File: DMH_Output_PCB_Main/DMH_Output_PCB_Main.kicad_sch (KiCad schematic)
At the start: 14 parts, among them J1 TS_Jack_6.35mm_Sw, J2 TS_Jack_6.35mm_Sw, J200 IDC_02x05, J21 Conn_01x02, J22 Conn_01x02, J24 Conn_01x02, J25 Conn_01x02, J3 TRS Jack 6.35mm, J4 TRS Jack 6.35mm, J5 TRS Jack 6.35mm, J6 TS_Jack_6.35mm_Sw, J7 TS_Jack_6.35mm_Sw, J8 TS_Jack_6.35mm_Sw, J9 TS_Jack_6.35mm_Sw

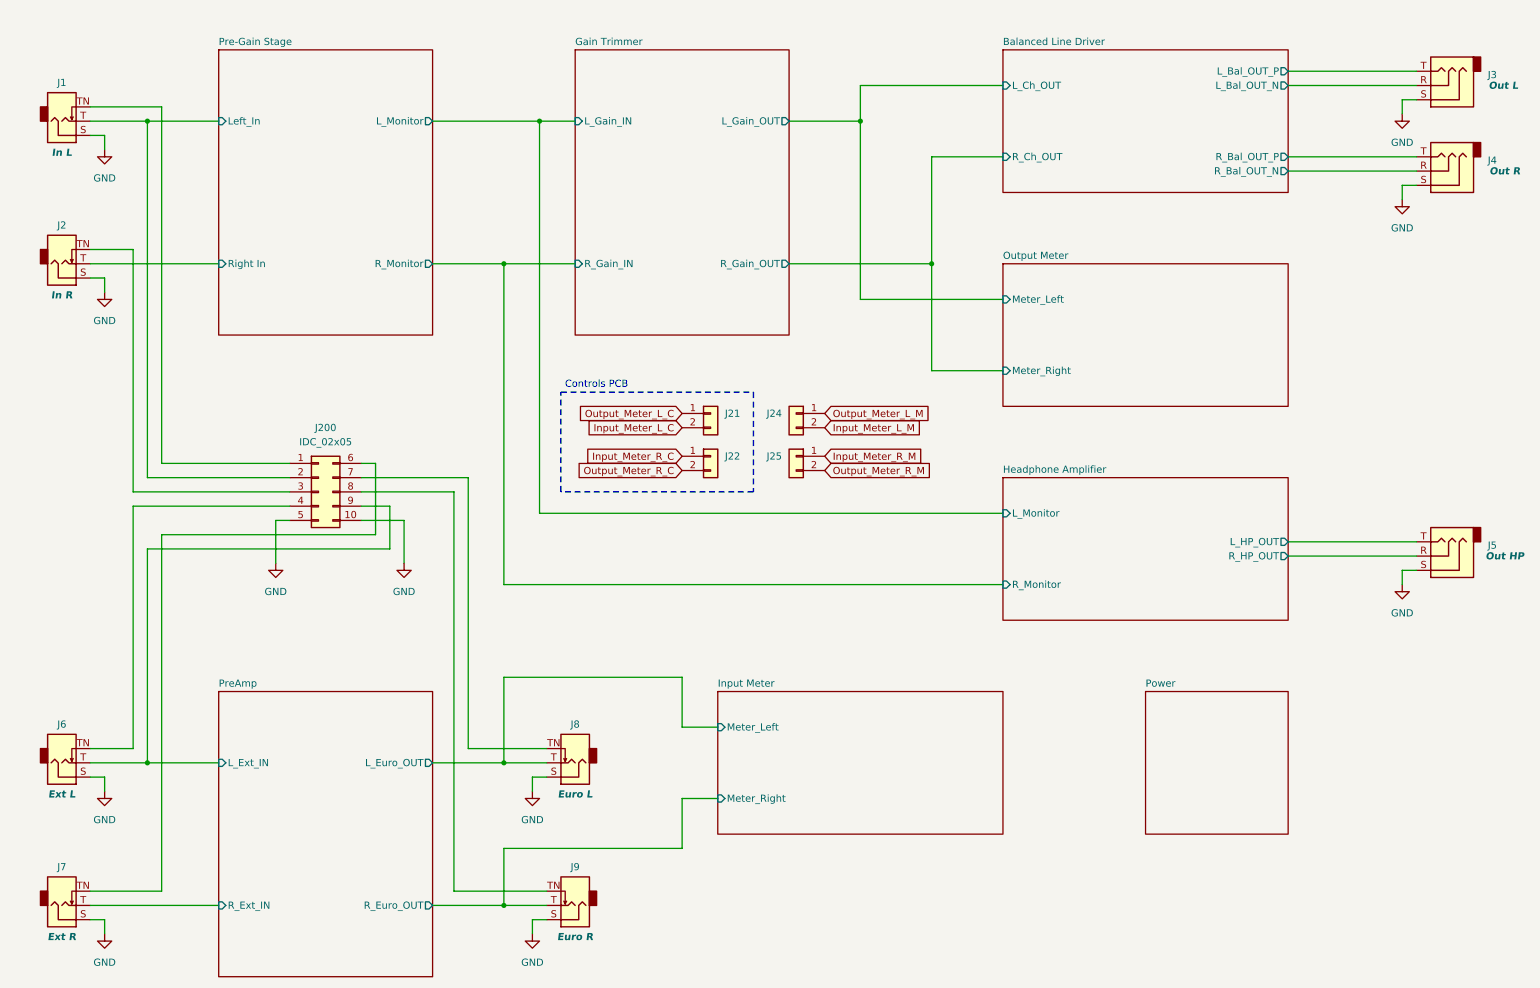
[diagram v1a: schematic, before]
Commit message: Replaced jack symbols with 5pin ones
Also updated Meter LED current source resistor to 75R
Also increased LED guiding PCB mounting holes to M2.5
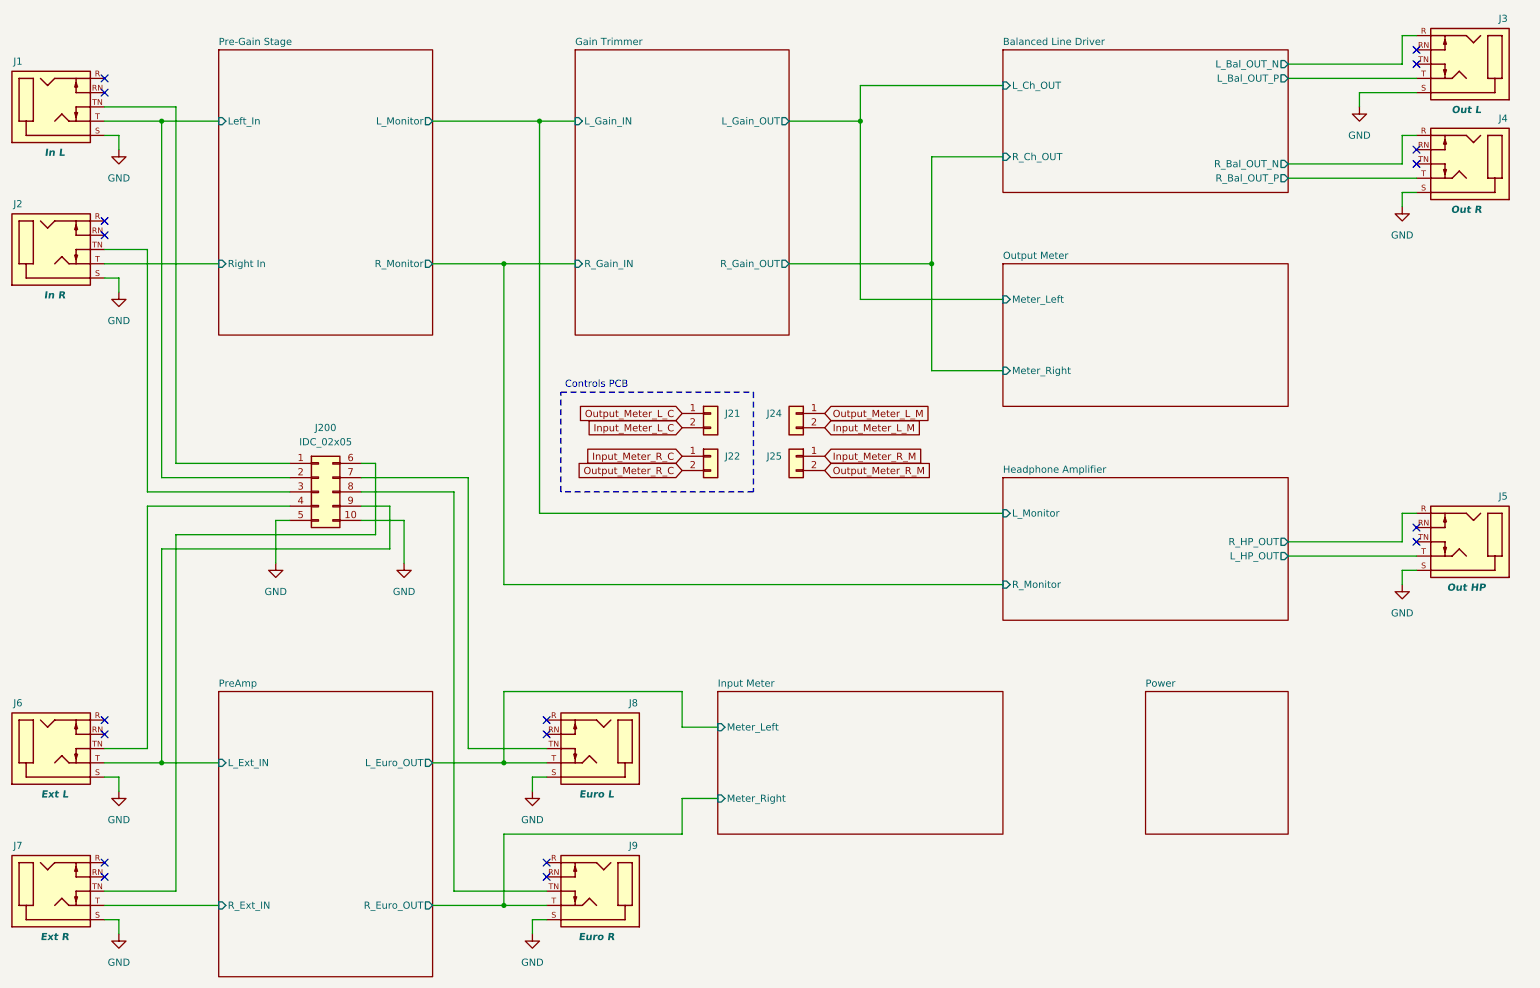
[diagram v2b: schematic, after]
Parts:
- J1, J2, J6, J7, J8, J9: value TS_Jack_6.35mm_Sw -> TRS_Jack_6.35mm_Sw; footprint SynthStuff:CUI_MJ-63052A -> SynthStuff:CUI_SJ-63083D; symbol SynthStuff:TS_Jack_6.35mm_Sw -> SynthStuff:TRS_Jack_6.35mm_Sw
- J3, J4, J5: value TRS Jack 6.35mm -> TRS_Jack_6.35mm_Sw; footprint SynthStuff:CUI_SJ-63083A -> SynthStuff:CUI_SJ-63083D; symbol Connector_Audio:AudioJack3 -> SynthStuff:TRS_Jack_6.35mm_Sw
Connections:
- no-connect marks 0 -> 18

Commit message: Prep for Main and MZ PCBs design in progress
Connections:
- net at J8.TN (2): now also J200.8 (Pin_8); no longer J200.7 (Pin_7)
- net at J2.TN (2): now also J200.1 (Pin_1); no longer J200.3 (Pin_3)
- net at J7.TN (2): now also J200.2 (Pin_2); no longer J200.6 (Pin_6)
- net at J9.TN (2): now also J200.9 (Pin_9); no longer J200.8 (Pin_8)
- net at J1.TN (2): now also J200.3 (Pin_3); no longer J200.1 (Pin_1)
- net Balanced Line Driver/L_Bal_OUT_N renamed Balanced Line Driver/L_Bal_OUT_N_M
- net Balanced Line Driver/L_Bal_OUT_P renamed Balanced Line Driver/L_Bal_OUT_P_M
- net Balanced Line Driver/R_Bal_OUT_N renamed Balanced Line Driver/R_Bal_OUT_N_M
- net Balanced Line Driver/R_Bal_OUT_P renamed Balanced Line Driver/R_Bal_OUT_P_M
- net Headphone Amplifier/L_HP_OUT renamed Headphone Amplifier/L_HP_OUT_M
- net Headphone Amplifier/R_HP_OUT renamed Headphone Amplifier/R_HP_OUT_M
- net Input Meter/Meter_Left renamed Input Meter/L_Ext_Meter_M
- net Input Meter/Meter_Right renamed Input Meter/R_Ext_Meter_M
- net Pre-Gain Stage/Left_In renamed Pre-Gain Stage/L_In_M
- net Pre-Gain Stage/L_In_M: now also J200.6 (Pin_6); no longer J200.2 (Pin_2)
- net Pre-Gain Stage/Right In renamed Pre-Gain Stage/R_In_M
- net PreAmp/L_Ext_IN renamed PreAmp/L_Ext_IN_M
- net PreAmp/L_Ext_IN_M: now also J200.7 (Pin_7); no longer J200.9 (Pin_9)
- net PreAmp/R_Ext_IN renamed PreAmp/R_Ext_IN_M
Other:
- sheet Balanced Line Driver ports: added L_Bal_OUT_N_M, L_Bal_OUT_P_M, L_Ch_OUT_M, R_Bal_OUT_N_M, R_Bal_OUT_P_M, R_Ch_OUT_M; removed L_Bal_OUT_N, L_Bal_OUT_P, L_Ch_OUT, R_Bal_OUT_N, R_Bal_OUT_P, R_Ch_OUT
- sheet Gain Trimmer ports: added L_Gain_IN_M, L_Gain_OUT_M, R_Gain_IN_M, R_Gain_OUT_M; removed L_Gain_IN, L_Gain_OUT, R_Gain_IN, R_Gain_OUT
- sheet Headphone Amplifier ports: added L_HP_IN_M, L_HP_OUT_M, R_HP_IN_M, R_HP_OUT_M; removed L_HP_OUT, L_Monitor, R_HP_OUT, R_Monitor
- sheet Input Meter ports: added L_Ext_Meter_M, R_Ext_Meter_M; removed Meter_Left, Meter_Right
- sheet Output Meter ports: added L_Out_Meter_M, R__Out_Meter_M; removed Meter_Left, Meter_Right
- sheet Pre-Gain Stage ports: added L_In_M, L_Monitor_M, R_In_M, R_Monitor_M; removed L_Monitor, Left_In, R_Monitor, Right In
- sheet PreAmp ports: added L_Euro_OUT_M, L_Ext_IN_M, R_Euro_OUT_M, R_Ext_IN_M; removed L_Euro_OUT, L_Ext_IN, R_Euro_OUT, R_Ext_IN

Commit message: Prepped for Main PCB design
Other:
- sheet Output Meter ports: added R_Out_Meter_M; removed R__Out_Meter_M
- note added: "Mezanine PCB"
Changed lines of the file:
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@@
 		)
 	)
+	(text "Mezanine PCB"
+		(exclude_from_sim no)
+		(at 69.85 138.43 0)
+		(effects
+			(font
+				(size 1.27 1.27)
+			)
+		)
+	)
+	(text "Mezanine PCB"
+		(exclude_from_sim no)
+		(at 220.98 24.13 0)
+		(effects
+			(font
+				(size 1.27 1.27)
+			)
+		)
+	)
+	(text "Mezanine PCB"
+		(exclude_from_sim no)
+		(at 74.93 24.13 0)
+		(effects
+			(font
+				(size 1.27 1.27)
+			)
+		)
+	)
 	(text_box "Install jumpers between J200 pins 1 and 6, and 2 and 7, to allow using In L and Ext L as Mono inputs"
 		(exclude_from_sim no)
@@
 			)
 		)
-		(pin "R__Out_Meter_M" input
+		(pin "R_Out_Meter_M" input
 			(at 190.5 82.55 180)
 			(effects

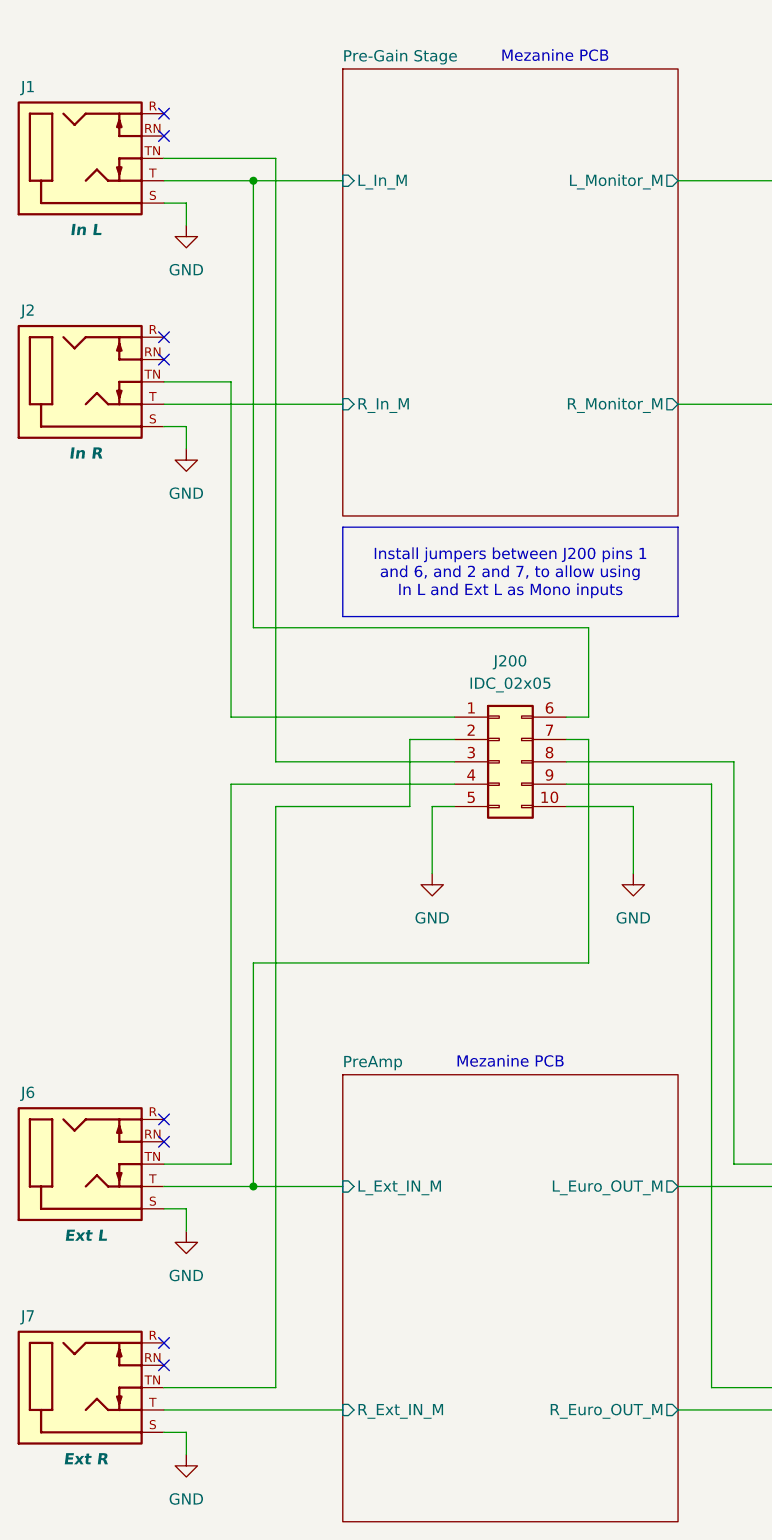
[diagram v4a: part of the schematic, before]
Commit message: Main PCB routing done
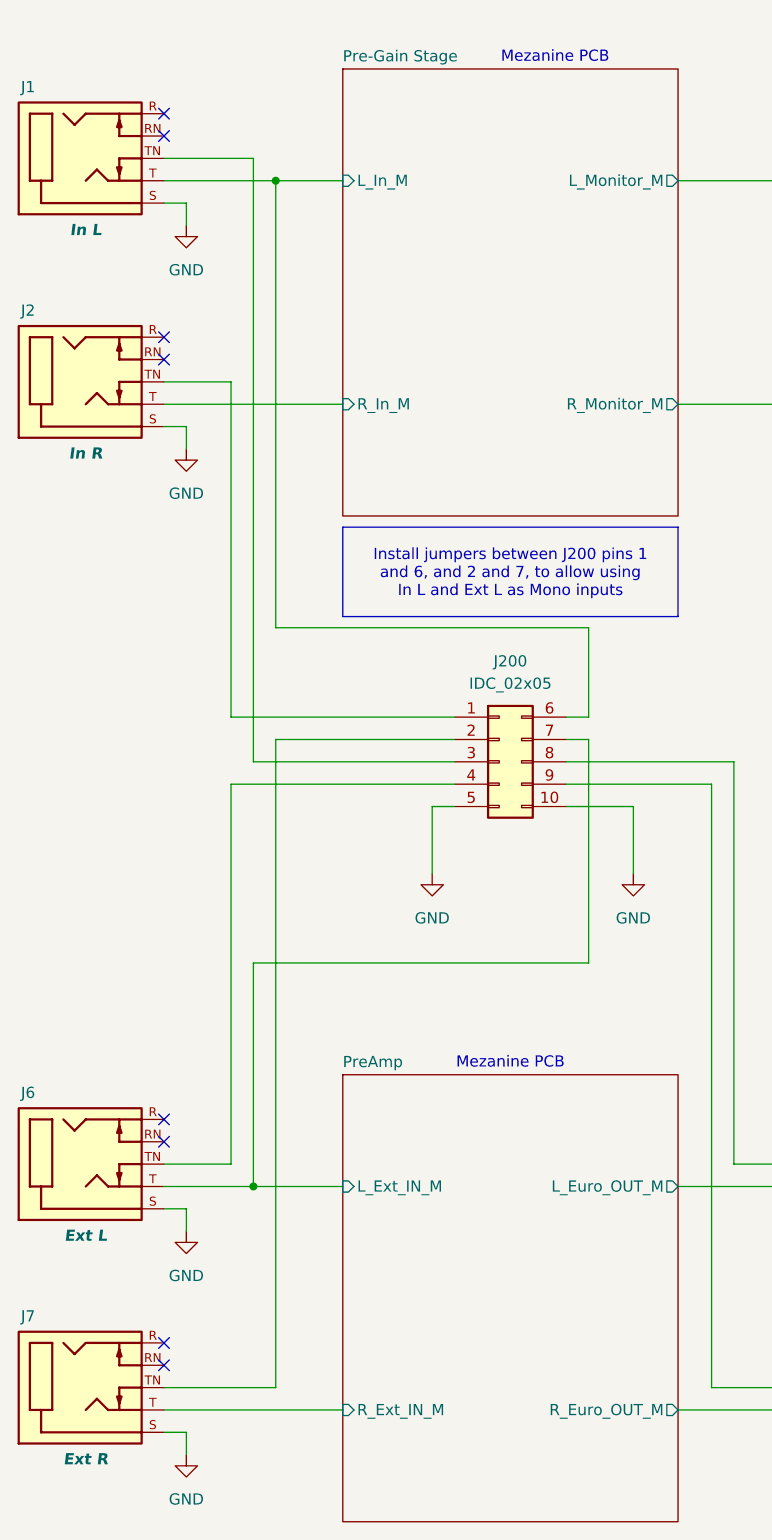
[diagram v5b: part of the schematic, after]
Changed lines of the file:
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@@
 	)
 	(junction
-		(at 40.64 38.1)
+		(at 43.18 38.1)
 		(diameter 0)
 		(color 0 0 0 0)
@@
 	(wire
 		(pts
-			(xy 40.64 38.1) (xy 50.8 38.1)
+			(xy 43.18 38.1) (xy 50.8 38.1)
 		)
 		(stroke
@@
 	(wire
 		(pts
-			(xy 58.42 101.6) (xy 63.5 101.6)
-		)
-		(stroke
-			(width 0)
-			(type default)
-		)
-	)
-	(wire
-		(pts
 			(xy 165.1 31.75) (xy 190.5 31.75)
 		)
@@
 	(wire
 		(pts
-			(xy 30.48 35.56) (xy 43.18 35.56)
+			(xy 30.48 35.56) (xy 40.64 35.56)
 		)
 		(stroke
@@
 	(wire
 		(pts
-			(xy 58.42 109.22) (xy 58.42 101.6)
-		)
-		(stroke
-			(width 0)
-			(type default)
-		)
-	)
-	(wire
-		(pts
 			(xy 261.62 107.95) (xy 264.16 107.95)
 		)
@@
 	(wire
 		(pts
-			(xy 40.64 88.9) (xy 40.64 38.1)
+			(xy 43.18 88.9) (xy 43.18 38.1)
 		)
 		(stroke
@@
 	(wire
 		(pts
-			(xy 43.18 104.14) (xy 63.5 104.14)
+			(xy 40.64 104.14) (xy 63.5 104.14)
 		)
 		(stroke
@@
 	(wire
 		(pts
-			(xy 40.64 88.9) (xy 78.74 88.9)
+			(xy 43.18 88.9) (xy 78.74 88.9)
 		)
 		(stroke
@@
 	(wire
 		(pts
-			(xy 43.18 35.56) (xy 43.18 104.14)
+			(xy 40.64 35.56) (xy 40.64 104.14)
 		)
 		(stroke
@@
 	(wire
 		(pts
-			(xy 43.18 109.22) (xy 43.18 175.26)
+			(xy 43.18 101.6) (xy 43.18 175.26)
 		)
 		(stroke
@@
 	(wire
 		(pts
-			(xy 30.48 38.1) (xy 40.64 38.1)
+			(xy 30.48 38.1) (xy 43.18 38.1)
 		)
 		(stroke
@@
 	(wire
 		(pts
-			(xy 43.18 109.22) (xy 58.42 109.22)
-		)
-		(stroke
+			(xy 43.18 101.6) (xy 63.5 101.6)
+		)
+		(stroke
